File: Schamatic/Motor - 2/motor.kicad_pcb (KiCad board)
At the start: 2 copper layers, 45 x 45 mm, 128 parts, among them J1 CONN_02X05, J11 V, J12 U, J13 W, J2 RS485, J3 RS485, J6 +BAT, J9 GND, SW1 B3U-1000P, SW2 B3U-1000P, U1 TPS73433DRV, U2 LTC2876, U3 ZXTR2012Z, U4 LM5019, U5 STM32F031K6U6, U6 A1335, U7 IRSM005, U8 IRSM005, U9 IRSM005, Y1 8MhZ

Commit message: fixing schematic errors
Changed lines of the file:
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@@
     (polygon
       (pts
-        (xy 57.5 88) (xy 57.5 83.65) (xy 52.65 76.75) (xy 51.3 76.25) (xy 49.3 76.2)
-        (xy 47.55 74.2) (xy 45.05 74.2) (xy 44.75 73.9) (xy 44.75 65.9) (xy 45.05 65.6)
-        (xy 48.7 65.6) (xy 49.05 65.95) (xy 49.05 68.7) (xy 52.5 68.7) (xy 52.7 68.5)
-        (xy 55.8 68.5) (xy 55.8 64.5) (xy 52.55 64.5) (xy 51.95 63.9) (xy 51.95 60.15)
-        (xy 52.35 59.75) (xy 54.65 59.75) (xy 54.65 56.35) (xy 48.85 56.35) (xy 48.85 62.75)
-        (xy 48.15 63.45) (xy 43.25 63.45) (xy 43.05 63.65) (xy 43 75.65) (xy 43.75 76.35)
-        (xy 46.65 76.35) (xy 48.6 78.55) (xy 51.45 78.55) (xy 55.05 83.7) (xy 55.05 88)
+        (xy 57.5 88) (xy 57.5 77.898044) (xy 45.05 74.45) (xy 44.75 74.15) (xy 44.75 65.9)
+        (xy 45.05 65.6) (xy 48.7 65.6) (xy 49.05 65.95) (xy 49.05 68.7) (xy 52.5 68.7)
+        (xy 52.7 68.5) (xy 55.8 68.5) (xy 55.8 64.5) (xy 52.55 64.5) (xy 51.95 63.9)
+        (xy 51.95 60.15) (xy 52.35 59.75) (xy 54.65 59.75) (xy 54.65 56.35) (xy 48.85 56.35)
+        (xy 48.85 62.75) (xy 48.15 63.45) (xy 43.25 63.45) (xy 43.05 63.65) (xy 43 75.65)
+        (xy 43.75 76.35) (xy 55.05 79.2) (xy 55.05 88)
       )
     )
@@
     )
   )
-  (zone (net 0) (net_name "") (layer F.SilkS) (hatch edge 0.508)
+  (zone (net 0) (net_name "") (layer F.Mask) (hatch edge 0.508)
+    (priority 1)
     (connect_pads yes (clearance 0.2))
     (min_thickness 0.254)
@@
       )
     )
+  )
+  (zone (net 0) (net_name "") (layer F.Mask) (hatch edge 0.508)
+    (priority 1)
+    (connect_pads yes (clearance 0.2))
+    (min_thickness 0.254)
+    (fill yes (arc_segments 32) (thermal_gap 0.508) (thermal_bridge_width 0.508))
+    (polygon
+      (pts
+        (xy 57.5 88) (xy 57.5 77.9) (xy 54.4 77.075) (xy 45.05 74.45) (xy 44.75 74.15)
+        (xy 44.75 65.9) (xy 45.05 65.6) (xy 48.7 65.6) (xy 49.05 65.95) (xy 49.05 68.7)
+        (xy 52.5 68.7) (xy 52.7 68.5) (xy 55.8 68.5) (xy 55.8 64.5) (xy 52.55 64.5)
+        (xy 51.95 63.9) (xy 51.95 60.15) (xy 52.35 59.75) (xy 54.65 59.75) (xy 54.65 56.35)
+        (xy 48.85 56.35) (xy 48.85 62.75) (xy 48.15 63.45) (xy 43.25 63.45) (xy 43.05 63.65)
+        (xy 43 75.65) (xy 43.75 76.35) (xy 55.05 79.2) (xy 55.05 88)
+      )
+    )
+  )
+  (zone (net 0) (net_name "") (layer B.Mask) (hatch edge 0.508)
+    (priority 1)
+    (connect_pads yes (clearance 0.2))
+    (min_thickness 0.254)
+    (fill yes (arc_segments 32) (thermal_gap 0.508) (thermal_bridge_width 0.508))
+    (polygon
+      (pts
+        (xy 68.45 86.75) (xy 68.45 71.35) (xy 62.05 67.65) (xy 59.55 58.1) (xy 58 56.35)
+        (xy 55.3 56.35) (xy 55.3 59.7) (xy 58.1 59.7) (xy 60.45 68.5) (xy 66.7 72.15)
+        (xy 66.7 86.75)
+      )
+    )
+  )
+  (zone (net 0) (net_name "") (layer B.Mask) (hatch edge 0.508)
+    (priority 1)
+    (connect_pads yes (clearance 0.2))
+    (min_thickness 0.254)
+    (fill yes (arc_segments 32) (thermal_gap 0.508) (thermal_bridge_width 0.508))
+    (polygon
+      (pts
+        (xy 65.9 86.75) (xy 65.9 72.15) (xy 59.2 68.5) (xy 59.2 65.15) (xy 56.5 65.1)
+        (xy 56.5 68.55) (xy 64.15 72.65) (xy 64.15 86.75)
+      )
+    )
+  )
+  (zone (net 0) (net_name "") (layer B.Mask) (hatch edge 0.508)
+    (priority 1)
+    (connect_pads yes (clearance 0.2))
+    (min_thickness 0.254)
+    (fill yes (arc_segments 32) (thermal_gap 0.508) (thermal_bridge_width 0.508))
+    (polygon
+      (pts
+        (xy 63.35 86.75) (xy 63.35 84.7) (xy 52.5 69.3) (xy 49.1 69.3) (xy 49.1 72.05)
+        (xy 52.15 72.05) (xy 61.65 85.8) (xy 61.65 86.75)
+      )
+    )

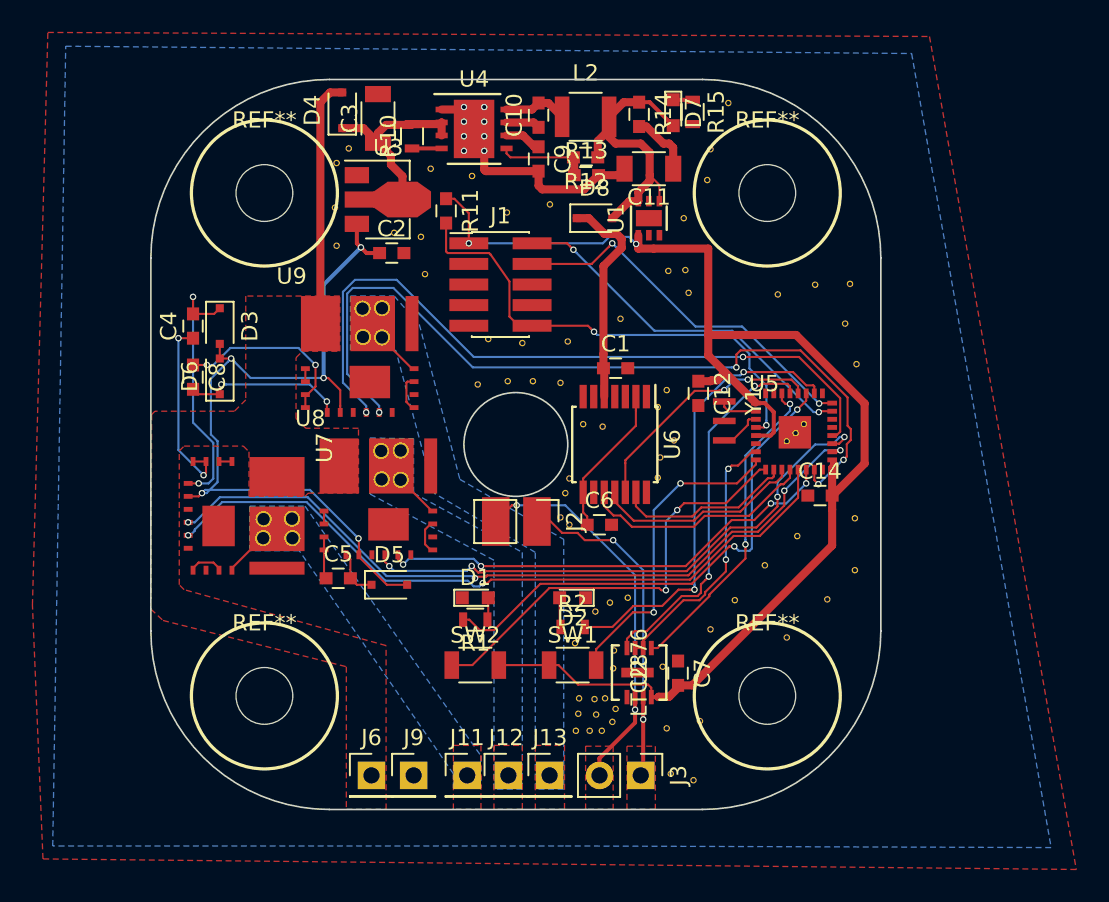
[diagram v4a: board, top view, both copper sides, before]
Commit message: problems with A1335 linearization, back to M700
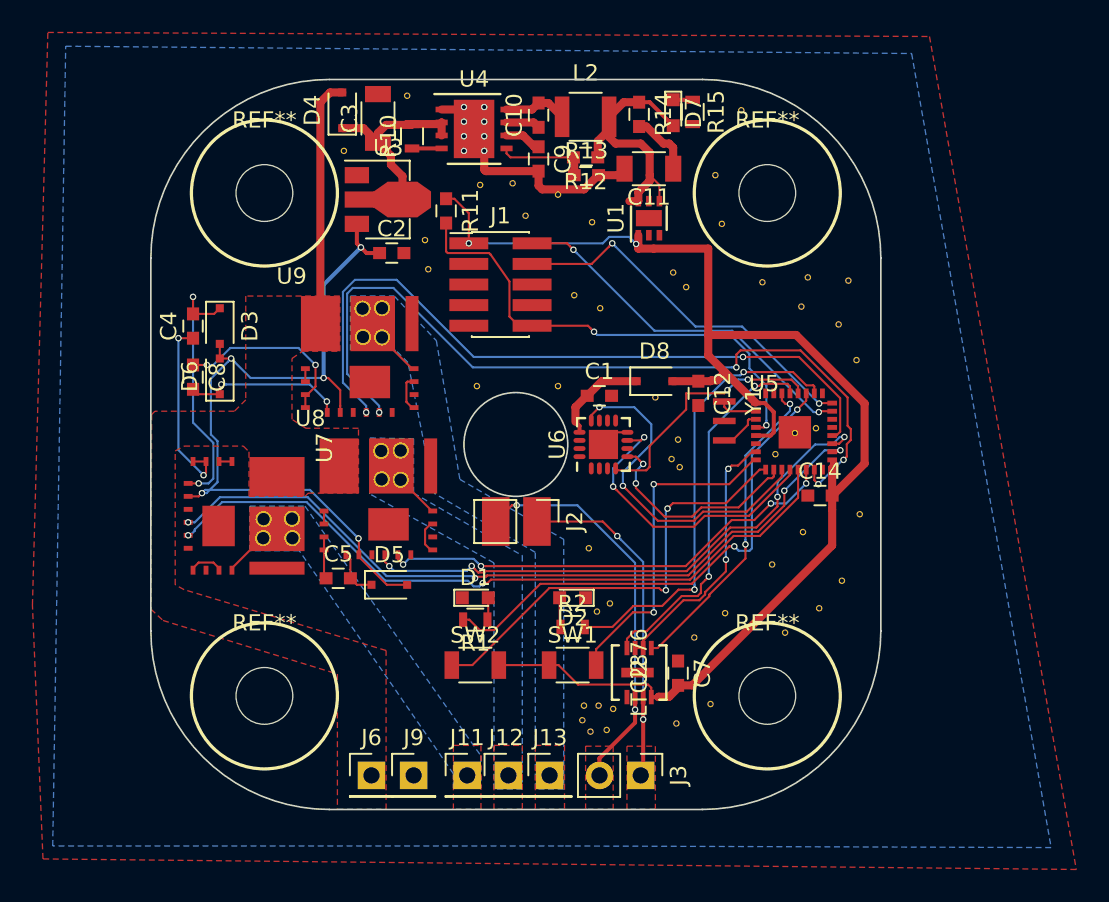
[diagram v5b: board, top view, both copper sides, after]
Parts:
- removed C6: 0.1uF, Capacitors_SMD:C_0603
- removed the REF** at (68.9, 67.6)
- removed the REF** at (71.1, 81.2)
- removed the REF** at (70.5, 81.2)
- removed the REF** at (69.5, 81.2)
- removed the REF** at (83.3, 64.2)
- removed the REF** at (82.8, 64.8)
- removed the REF** at (82.3, 65.3)
- removed the REF** at (74.3, 67.5)
- removed the REF** at (74.5, 66.3)
- removed the REF** at (75.3, 65.2)
- removed the REF** at (74.3, 63.2)
- removed the REF** at (68.9, 70.5)
- removed the REF** at (74.9, 62.1)
- removed the REF** at (78.7, 44.5)
- removed the REF** at (77.6, 47.3)
- removed the REF** at (77.4, 49.2)
- removed the REF** at (76.0, 51.5)
- removed the REF** at (67.7, 50.7)
- removed the REF** at (65.0, 51.2)
- removed the REF** at (62.9, 49.0)
- removed the REF** at (60.4, 48.5)
- removed the REF** at (55.3, 47.2)
- removed the REF** at (70.5, 82.2)
- removed the REF** at (54.5, 48.1)
- removed the REF** at (54.5, 50.9)
- removed the REF** at (54.5, 53.2)
- removed the REF** at (58.1, 52.5)
- removed the REF** at (59.8, 52.7)
- removed the REF** at (60.0, 55.0)
- removed the REF** at (76.5, 86.2)
- removed the REF** at (75.2, 85.8)
- removed the REF** at (74.9, 83.0)
- removed the REF** at (77.0, 82.5)
- removed the REF** at (69.5, 82.1)
- removed the REF** at (82.3, 77.4)
- removed the REF** at (84.8, 75.0)
- removed the REF** at (86.5, 73.2)
- removed the REF** at (86.5, 70.0)
- removed the REF** at (83.0, 71.2)
- removed the REF** at (81.0, 73.0)
- removed the REF** at (79.1, 75.1)
- removed the REF** at (77.6, 76.9)
- removed the REF** at (74.7, 79.2)
- removed the REF** at (71.6, 79.3)
- removed the REF** at (69.3, 83.2)
- removed the REF** at (71.7, 78.2)
- removed the REF** at (69.2, 77.8)
- removed the REF** at (70.5, 75.8)
- removed the REF** at (72.5, 75.0)
- removed the REF** at (71.4, 75.2)
- removed the REF** at (68.3, 70.0)
- removed the REF** at (68.7, 68.5)
- removed the REF** at (71.0, 64.4)
- removed the REF** at (69.8, 64.2)
- removed the REF** at (68.3, 61.7)
- removed the REF** at (70.2, 83.2)
- removed the REF** at (66.7, 61.6)
- removed the REF** at (65.1, 61.6)
- removed the REF** at (63.2, 61.8)
- removed the REF** at (63.9, 59.0)
- removed the REF** at (66.0, 59.2)
- removed the REF** at (68.8, 59.1)
- removed the REF** at (72.0, 57.8)
- removed the REF** at (86.6, 60.5)
- removed the REF** at (76.2, 56.1)
- removed the REF** at (76.0, 54.8)
- removed the REF** at (70.9, 83.2)
- removed the REF** at (75.0, 54.8)
- removed the REF** at (86.2, 55.6)
- removed the REF** at (85.9, 58.0)
- removed the REF** at (84.0, 55.6)
- removed the REF** at (81.8, 56.2)
- removed the REF** at (71.5, 82.6)
- removed the REF** at (71.8, 81.8)
- added REF**: VIA-0.4, Dizzy:VIA-0.4, F.Cu at (86.6, 60.3)
- added REF**: VIA-0.4, Dizzy:VIA-0.4, F.Cu at (71.2, 83.1)
- added REF**: VIA-0.4, Dizzy:VIA-0.4, F.Cu at (71.6, 81.8)
- added REF**: VIA-0.4, Dizzy:VIA-0.4, F.Cu at (70.7, 81.6)
- added REF**: VIA-0.4, Dizzy:VIA-0.4, F.Cu at (69.8, 81.6)
- added REF**: VIA-0.4, Dizzy:VIA-0.4, F.Cu at (75.5, 82.7)
- added REF**: VIA-0.4, Dizzy:VIA-0.4, F.Cu at (77.6, 81.5)
- added REF**: VIA-0.4, Dizzy:VIA-0.4, F.Cu at (82.2, 77.1)
- added REF**: VIA-0.4, Dizzy:VIA-0.4, F.Cu at (84.3, 75.6)
- added REF**: VIA-0.4, Dizzy:VIA-0.4, F.Cu at (85.7, 73.9)
- added REF**: VIA-0.4, Dizzy:VIA-0.4, F.Cu at (86.8, 69.8)
- added REF**: VIA-0.4, Dizzy:VIA-0.4, F.Cu at (84.1, 64.5)
- added REF**: VIA-0.4, Dizzy:VIA-0.4, F.Cu at (83.3, 70.9)
- added REF**: VIA-0.4, Dizzy:VIA-0.4, F.Cu at (81.4, 72.9)
- added REF**: VIA-0.4, Dizzy:VIA-0.4, F.Cu at (78.5, 75.9)
- added REF**: VIA-0.4, Dizzy:VIA-0.4, F.Cu at (76.6, 77.4)
- added REF**: VIA-0.4, Dizzy:VIA-0.4, F.Cu at (70.1, 71.9)
- added REF**: VIA-0.4, Dizzy:VIA-0.4, F.Cu at (70.6, 75.8)
- added REF**: VIA-0.4, Dizzy:VIA-0.4, F.Cu at (71.4, 75.3)
- added REF**: VIA-0.4, Dizzy:VIA-0.4, F.Cu at (63.2, 61.9)
- added REF**: VIA-0.4, Dizzy:VIA-0.4, F.Cu at (68.2, 61.9)
- added REF**: VIA-0.4, Dizzy:VIA-0.4, F.Cu at (74.2, 62.6)
- added REF**: VIA-0.4, Dizzy:VIA-0.4, F.Cu at (81.6, 66.1)
- added REF**: VIA-0.4, Dizzy:VIA-0.4, F.Cu at (76.1, 55.8)
- added REF**: VIA-0.4, Dizzy:VIA-0.4, F.Cu at (75.3, 54.9)
- added REF**: VIA-0.4, Dizzy:VIA-0.4, F.Cu at (70.8, 57.1)
- added REF**: VIA-0.4, Dizzy:VIA-0.4, F.Cu at (69.2, 56.3)
- added REF**: VIA-0.4, Dizzy:VIA-0.4, F.Cu at (55.0, 47.4)
- added REF**: VIA-0.4, Dizzy:VIA-0.4, F.Cu at (60.0, 52.9)
- added REF**: VIA-0.4, Dizzy:VIA-0.4, F.Cu at (60.2, 54.7)
- added REF**: VIA-0.4, Dizzy:VIA-0.4, F.Cu at (58.9, 44.0)
- added REF**: VIA-0.4, Dizzy:VIA-0.4, F.Cu at (68.2, 50.1)
- added REF**: VIA-0.4, Dizzy:VIA-0.4, F.Cu at (65.4, 49.4)
- added REF**: VIA-0.4, Dizzy:VIA-0.4, F.Cu at (82.8, 64.8)
- added REF**: VIA-0.4, Dizzy:VIA-0.4, F.Cu at (63.4, 49.5)
- added REF**: VIA-0.4, Dizzy:VIA-0.4, F.Cu at (66.2, 51.4)
- added REF**: VIA-0.4, Dizzy:VIA-0.4, F.Cu at (70.3, 51.8)
- added REF**: VIA-0.4, Dizzy:VIA-0.4, F.Cu at (78.3, 51.9)
- added REF**: VIA-0.4, Dizzy:VIA-0.4, F.Cu at (77.9, 48.9)
- added REF**: VIA-0.4, Dizzy:VIA-0.4, F.Cu at (79.5, 44.9)
- added REF**: VIA-0.4, Dizzy:VIA-0.4, F.Cu at (85.5, 58.1)
- added REF**: VIA-0.4, Dizzy:VIA-0.4, F.Cu at (83.2, 57.0)
- added REF**: VIA-0.4, Dizzy:VIA-0.4, F.Cu at (80.8, 55.5)
- added REF**: VIA-0.4, Dizzy:VIA-0.4, F.Cu at (83.6, 55.2)
- added REF**: VIA-0.4, Dizzy:VIA-0.4, F.Cu at (75.7, 66.9)
- added REF**: VIA-0.4, Dizzy:VIA-0.4, F.Cu at (86.1, 55.4)
- added REF**: VIA-0.4, Dizzy:VIA-0.4, F.Cu at (75.6, 65.2)
- added REF**: VIA-0.4, Dizzy:VIA-0.4, F.Cu at (75.2, 66.4)
- added REF**: VIA-0.4, Dizzy:VIA-0.4, F.Cu at (69.7, 82.5)
- added REF**: VIA-0.4, Dizzy:VIA-0.4, F.Cu at (70.2, 83.2)
- U6: value A1335 -> MA700; footprint Housings_SSOP:TSSOP-14_4.4x5mm_Pitch0.65mm -> Housings_DFN_QFN:QFN-16-1EP_3x3mm_Pitch0.5mm
- moved D8 10.7 mm to (74.0, 61.6)
- moved C1 1.97 mm to (70.7, 62.5)
- moved U6 0.70 mm to (70.9, 65.5), turned to 90 degrees
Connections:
- C1 pad 1: 5V -> Net-(C1-Pad1)
- D8 pad 1: 5V -> Net-(C1-Pad1)
- D8 pad 2: Net-(D7-Pad2) -> +3V3
- U6 pad 1: Earth -> (no net)
- U6 pad 10: MISO -> (no net)
- U6 pad 11: SCK -> (no net)
- U6 pad 12: MOSI -> SCK
- U6 pad 13: CS -> Net-(C1-Pad1)
- U6 pad 14: Earth -> (no net)
- U6 pad 2: Net-(C6-Pad1) -> (no net)
- U6 pad 3: Earth -> (no net)
- U6 pad 4: (no net) -> MOSI
- U6 pad 5: 5V -> CS
- U6 pad 7: Earth -> MISO
- U6 pad 8: Net-(C6-Pad1) -> Earth
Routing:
- net 5V: track 13.5 -> 0.00 mm
- net Net-(C6-Pad1): track 9.99 -> 0.00 mm
- net SCK: track 12.9 -> 21.4 mm, vias 0 -> 2
- net Net-(C1-Pad1): track 0.00 -> 6.09 mm
- net MISO: track 14.6 -> 18.5 mm, vias 0 -> 2
- net Earth: track 20.7 -> 23.6 mm
- net CS: track 11.1 -> 13.5 mm, vias 0 -> 2
- net +3V3: track 85.2 -> 86.8 mm
- net Net-(D7-Pad2): track 19.0 -> 17.5 mm
- net Net-(SW1-Pad2): track 19.5 -> 20.3 mm
- added copper zone on F.Cu, net Net-(J11-Pad1)
- added copper zone on F.Cu, net Net-(J12-Pad1)
- added copper zone on F.Cu, net Net-(J13-Pad1)
- removed copper zone on F.Cu, net O1
- removed copper zone on F.Cu, net O2
- removed copper zone on F.Cu, net O3
